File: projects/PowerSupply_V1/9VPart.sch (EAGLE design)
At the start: 10 parts, among them IC1 LM2596T, X1 IN, X3 OUT

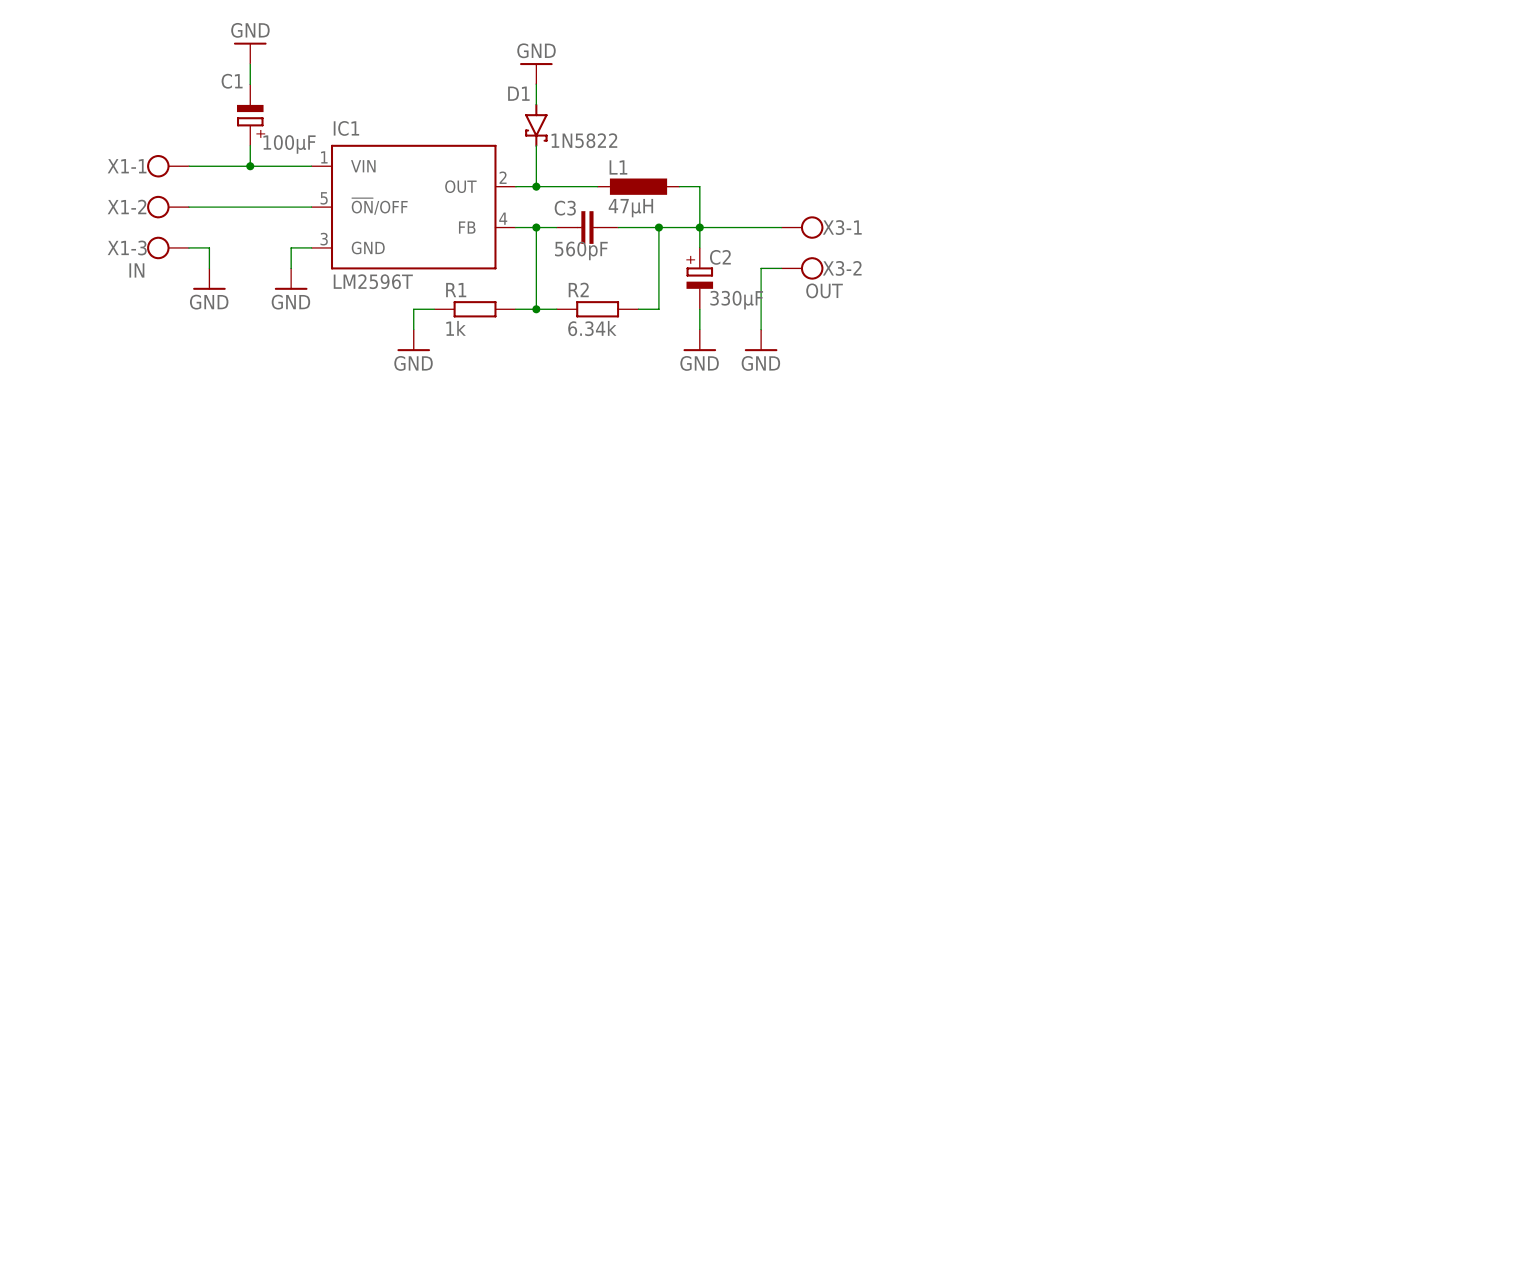
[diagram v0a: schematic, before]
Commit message: feat: power supply
changes:
- version one done
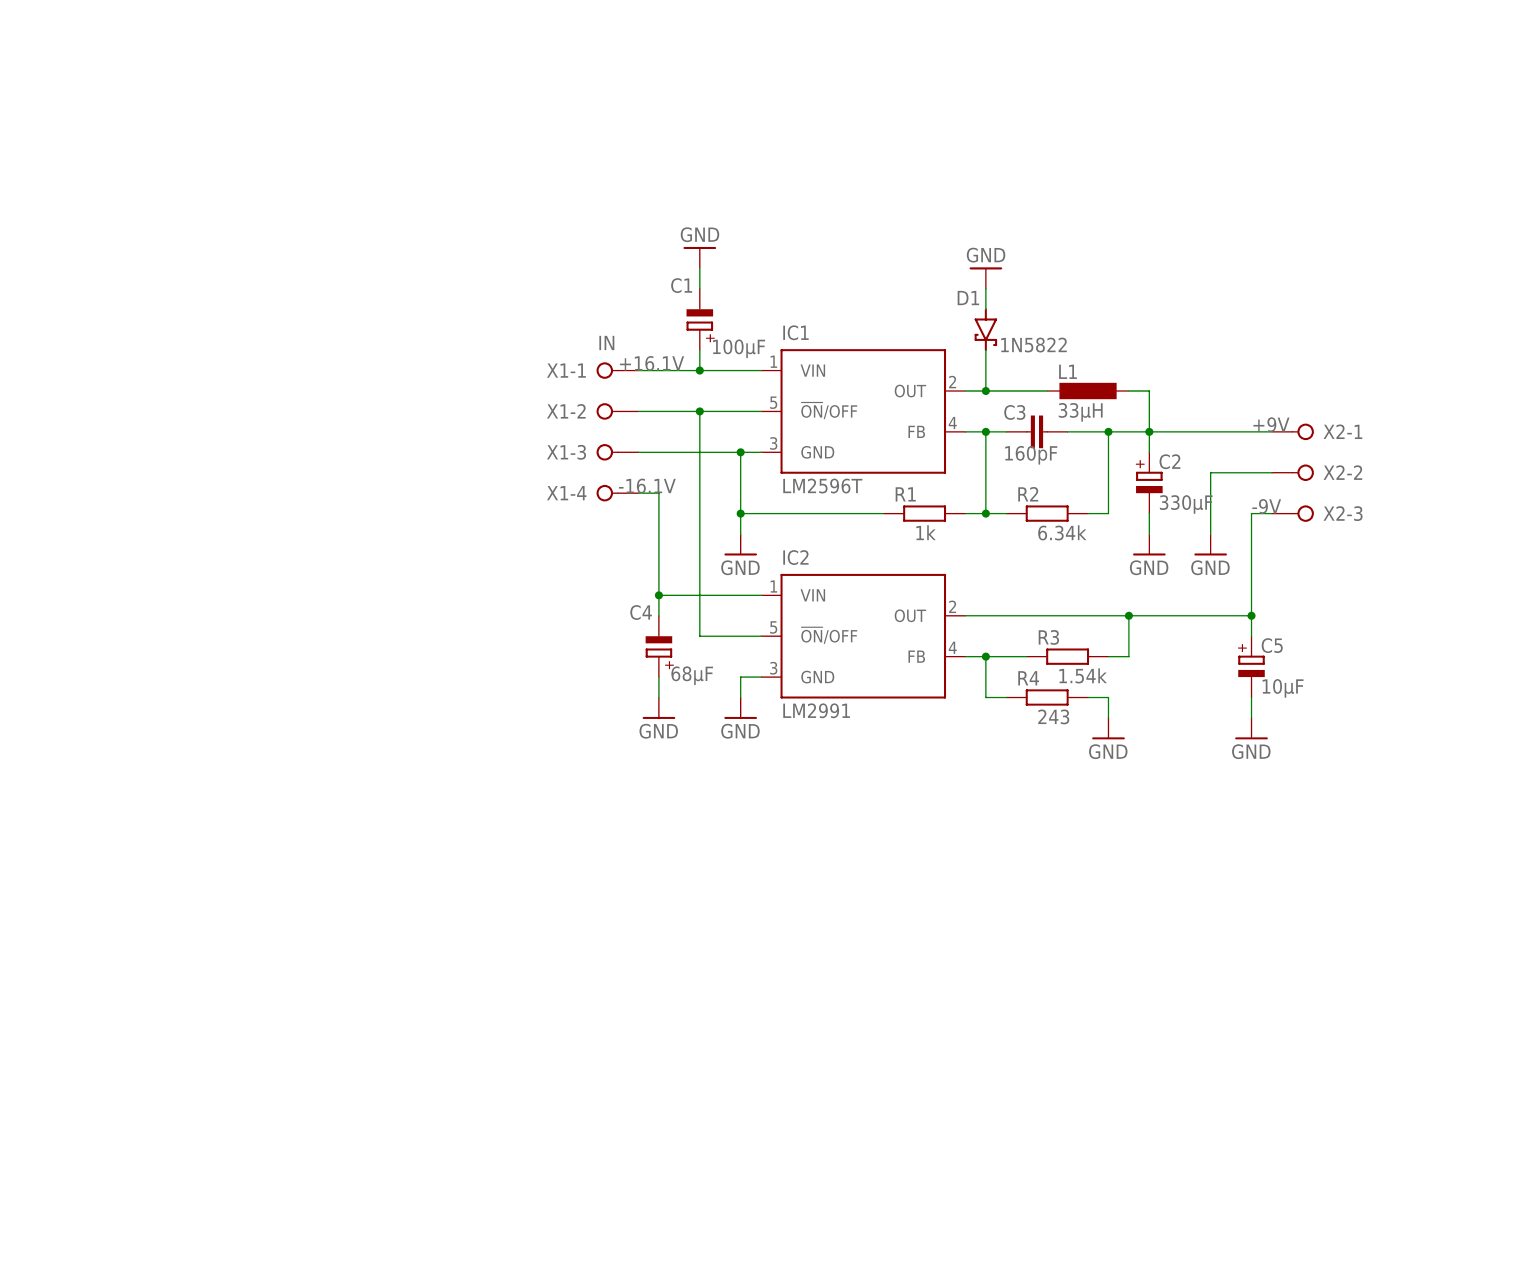
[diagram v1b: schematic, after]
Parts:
- removed X3: OUT, con-wago-500:W237-102
- added C4: 68µF, rcl:CPOL-EUE2.5-6
- added C5: 10µF, rcl:CPOL-EUE2.5-6
- added IC2: LM2991, national-semiconductor:LM2596T
- added R3: 1.54k, rcl:R-EU_0207/10
- added R4: 243, rcl:R-EU_0207/10
- added X2: (no value), con-wago-508:W237-03P
- C2: device rcl:CPOL-EUE3.5-8 -> rcl:CPOL-EUE2.5-6
- C3: value 560pF -> 160pF
- L1: value 47µH -> 33µH
- X1: device con-wago-500:W237-103 -> con-wago-508:W237-04P
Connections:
- net N$5 renamed +16.1V
- new net +9V: C2.+, C3.2, L1.1, R2.2, X2-1.KL
- new net -16.1V: C4.-, IC2.VIN, X1-4.KL
- new net -9V: C5.+, IC2.OUT, R3.2, X2-3.KL
- net GND: now also C4.+, C5.-, IC2.GND, R4.2, X2-2.KL; no longer X3-2.KL
- net N$2: now also IC2.!ON!/OFF
- net N$3: now also IC2.FB, R3.1, R4.1; no longer C2.+, C3.2, L1.1, R2.2, X3-1.KL
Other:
- moved on the sheet: C1, C2, C3, D1, IC1, L1, R1, R2

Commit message: feat: pwr fixes
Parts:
- C3: value 160pF -> 560pF
- C5: device rcl:CPOL-EUE2.5-6 -> rcl:CPOL-EUE1.8-4
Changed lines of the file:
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@@
 <part name="R1" library="rcl" library_urn="urn:adsk.eagle:library:334" deviceset="R-EU_" device="0207/10" package3d_urn="urn:adsk.eagle:package:23491/2" value="1k"/>
 <part name="R2" library="rcl" library_urn="urn:adsk.eagle:library:334" deviceset="R-EU_" device="0207/10" package3d_urn="urn:adsk.eagle:package:23491/2" value="6.34k"/>
-<part name="C3" library="rcl" library_urn="urn:adsk.eagle:library:334" deviceset="C-EU" device="050-024X044" package3d_urn="urn:adsk.eagle:package:23643/1" value="160pF"/>
+<part name="C3" library="rcl" library_urn="urn:adsk.eagle:library:334" deviceset="C-EU" device="050-024X044" package3d_urn="urn:adsk.eagle:package:23643/1" value="560pF"/>
 <part name="L1" library="rcl" library_urn="urn:adsk.eagle:library:334" deviceset="L-EU" device="TJ3-U2" package3d_urn="urn:adsk.eagle:package:23497/1" value="33µH"/>
 <part name="GND8" library="supply1" library_urn="urn:adsk.eagle:library:371" deviceset="GND" device=""/>
@@
 <part name="C4" library="rcl" library_urn="urn:adsk.eagle:library:334" deviceset="CPOL-EU" device="E2.5-6" package3d_urn="urn:adsk.eagle:package:23349/1" value="68µF"/>
 <part name="GND6" library="supply1" library_urn="urn:adsk.eagle:library:371" deviceset="GND" device=""/>
-<part name="C5" library="rcl" library_urn="urn:adsk.eagle:library:334" deviceset="CPOL-EU" device="E2.5-6" package3d_urn="urn:adsk.eagle:package:23349/1" value="10µF"/>
+<part name="C5" library="rcl" library_urn="urn:adsk.eagle:library:334" deviceset="CPOL-EU" device="E1.8-4" package3d_urn="urn:adsk.eagle:package:23336/2" value="10µF"/>
 <part name="GND7" library="supply1" library_urn="urn:adsk.eagle:library:371" deviceset="GND" device=""/>
 <part name="R3" library="rcl" library_urn="urn:adsk.eagle:library:334" deviceset="R-EU_" device="0207/10" package3d_urn="urn:adsk.eagle:package:23491/2" value="1.54k"/>

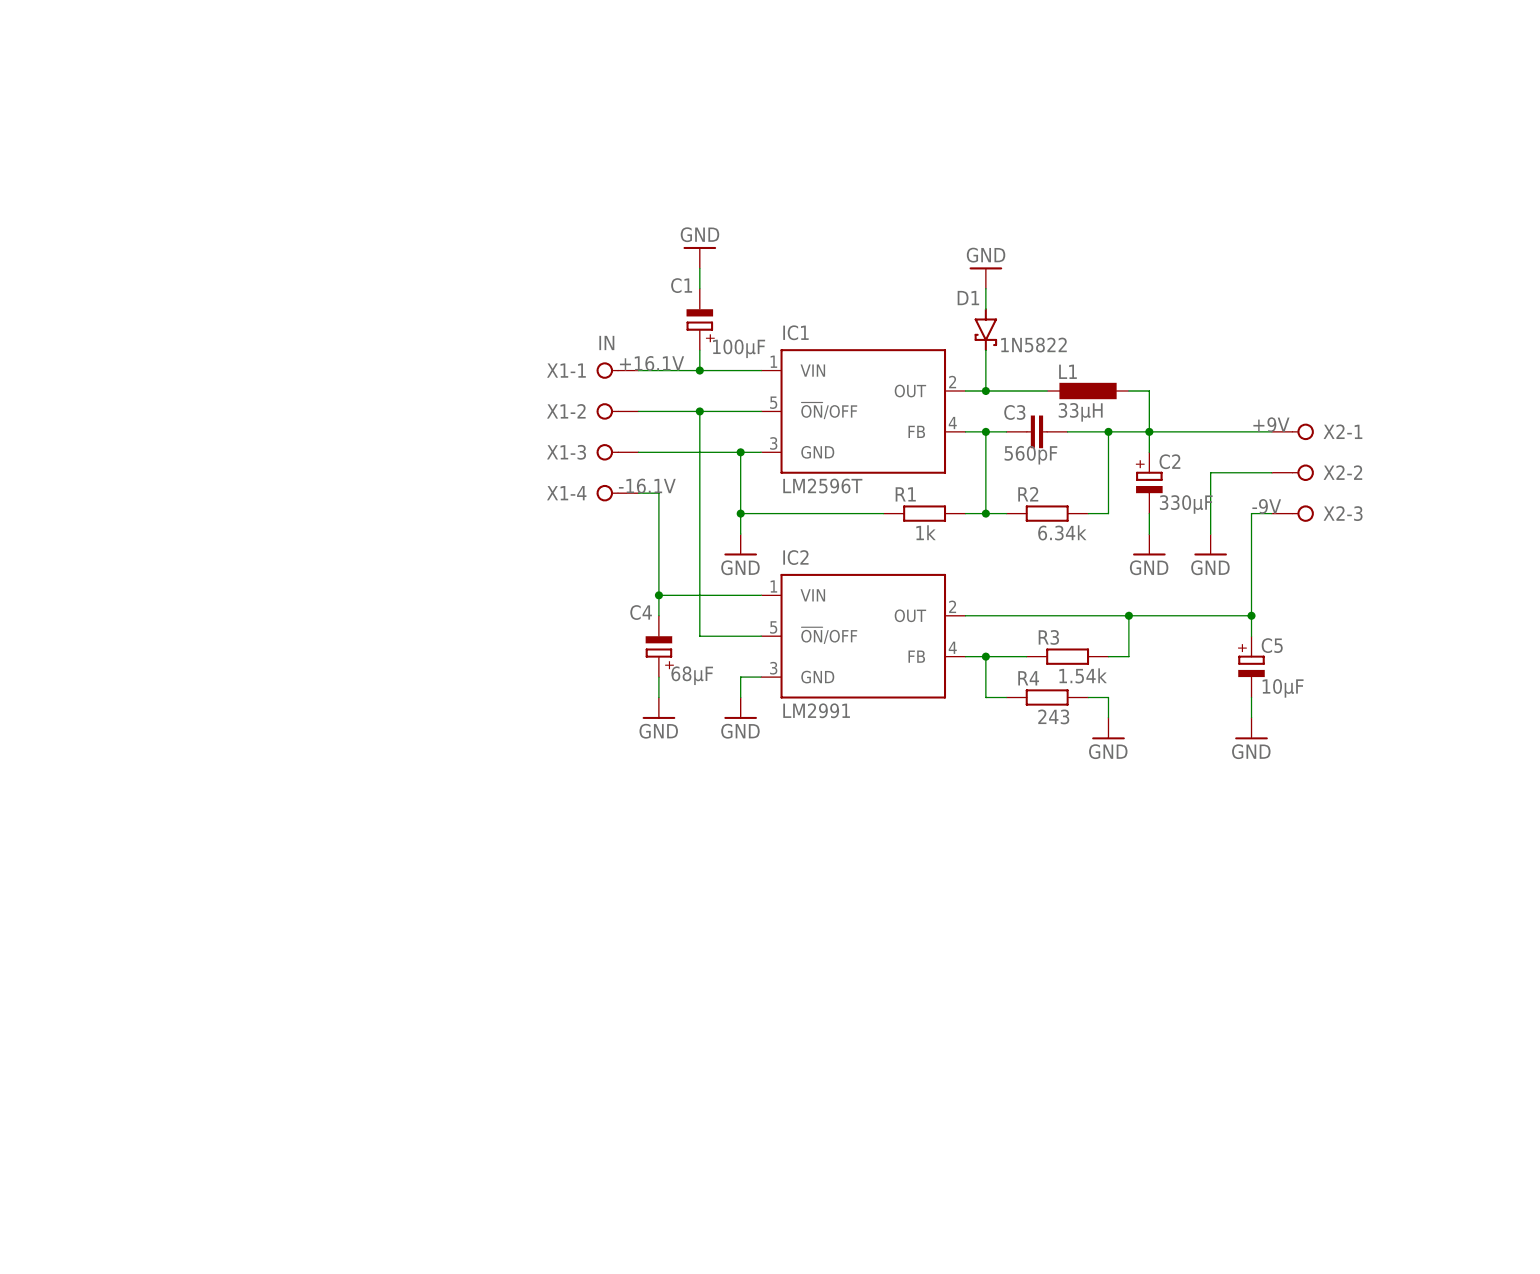
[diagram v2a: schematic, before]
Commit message: feat: 9V part refactored
changes:
- schematic changed
- layout changed
- gerber files added
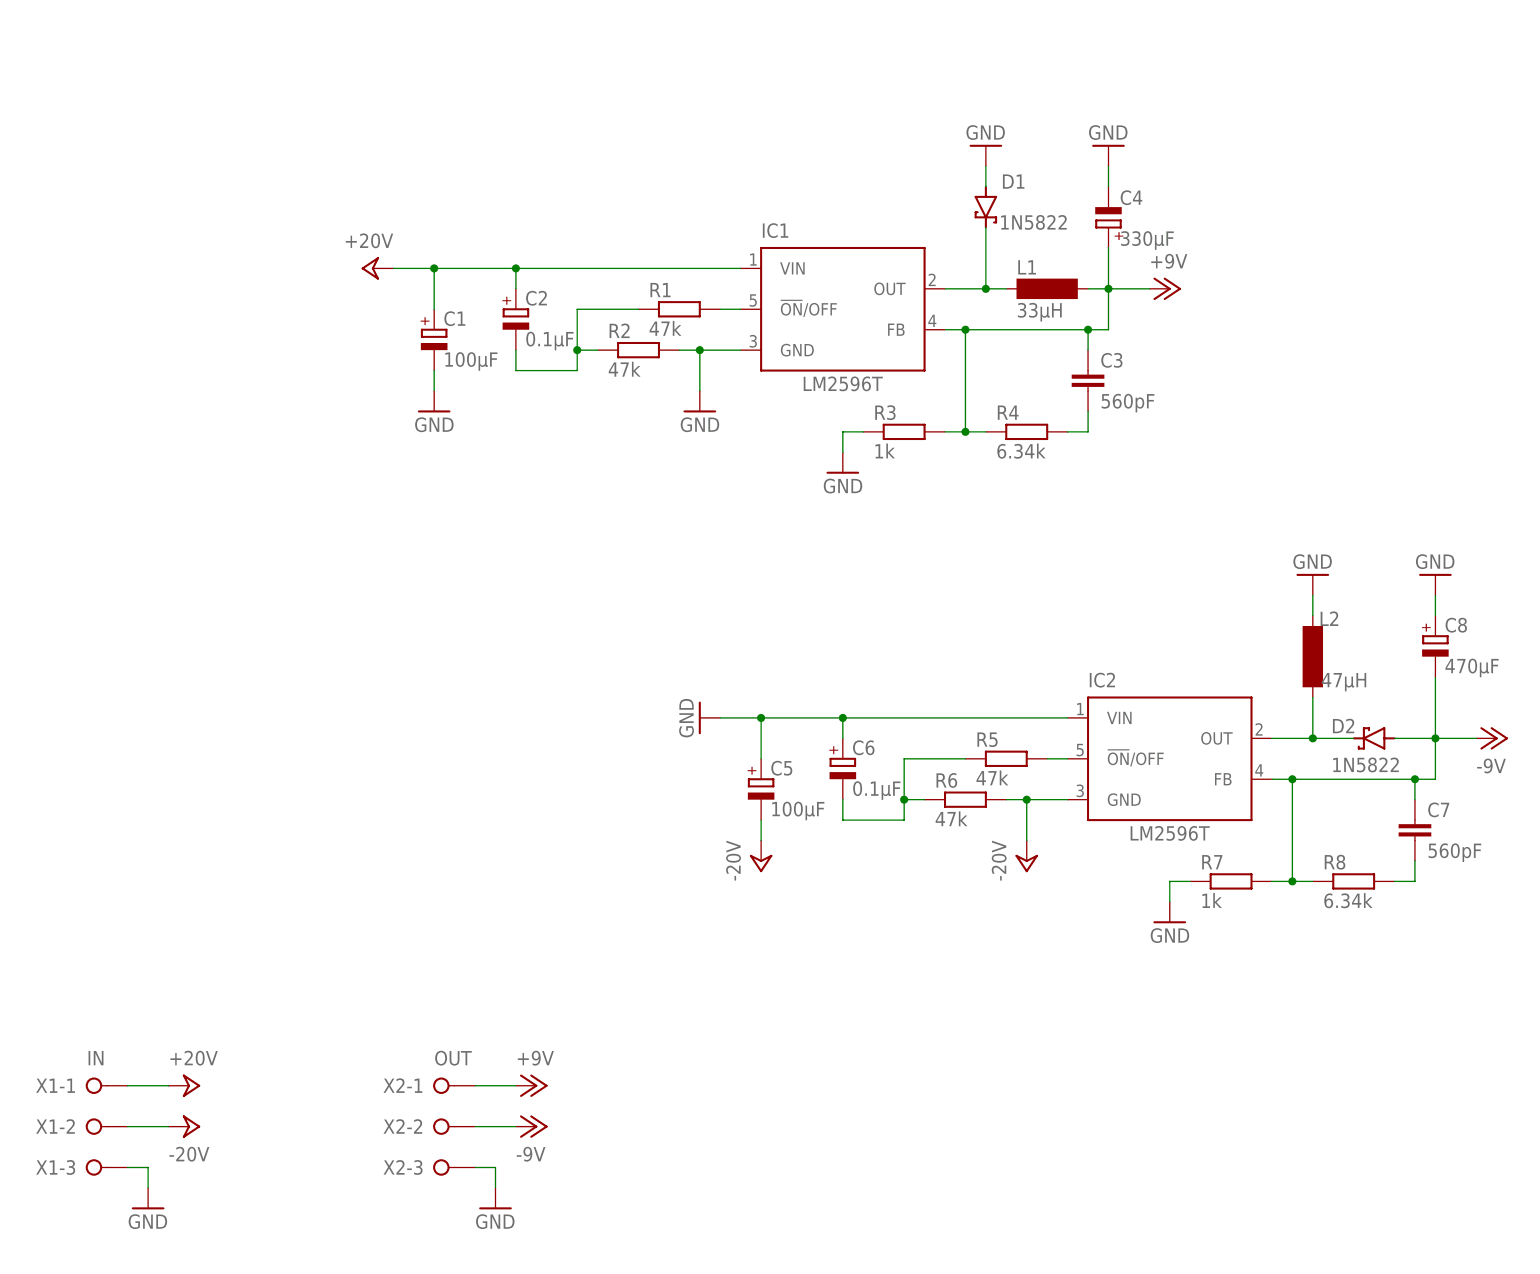
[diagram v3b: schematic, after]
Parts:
- added C6: 0.1µF, rcl:CPOL-EUE1.8-4
- added C7: 560pF, rcl:C-EU050-024X044
- added C8: 470µF, rcl:CPOL-EUE3.5-8
- added D2: 1N5822, diode:SCHOTTKY-DIODEC4111-15
- added L2: 47µH, inductor-neosid:SD12-680
- added R5, R6: 47k, rcl:R-EU_0207/10
- added R7: 1k, rcl:R-EU_0207/10
- added R8: 6.34k, rcl:R-EU_0207/10
- C2: value 330µF -> 0.1µF; device rcl:CPOL-EUE2.5-6 -> rcl:CPOL-EUE1.8-4
- C4: value 68µF -> 330µF; device rcl:CPOL-EUE2.5-6 -> rcl:CPOL-EUE3.5-8
- C5: value 10µF -> 100µF; device rcl:CPOL-EUE1.8-4 -> rcl:CPOL-EUE2.5-6
- IC2: value LM2991 -> LM2596T
- L1: device rcl:L-EUTJ3-U2 -> inductor-neosid:SD12-680
- R1: value 1k -> 47k
- R2: value 6.34k -> 47k
- R3: value 1.54k -> 1k
- R4: value 243 -> 6.34k
- X1: device con-wago-508:W237-04P -> con-wago-508:W237-03P
- X2: value (none) -> OUT
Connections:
- removed net +16.1V: C1.+, IC1.VIN, X1-1.KL
- removed net +9V: C2.+, C3.2, L1.1, R2.2, X2-1.KL
- removed net -16.1V: C4.-, IC2.VIN, X1-4.KL
- removed net -9V: C5.+, IC2.OUT, R3.2, X2-3.KL
- new net +12V: C3.1, C4.+, IC1.FB, L1.2, R3.2, R4.1, X2-1.KL
- new net +24V: C1.+, C2.+, IC1.VIN, X1-1.KL
- new net -12V: C7.1, C8.-, D2.A, IC2.FB, R7.2, R8.1, X2-2.KL
- new net -24V: C5.-, IC2.GND, R6.2, X1-2.KL
- new net N$5: C7.2, R8.2
- new net N$6: C2.-, R1.1, R2.1
- new net N$7: IC2.!ON!/OFF, R5.2
- new net N$8: C6.-, R5.1, R6.1
- net GND: now also C4.-, C5.+, C6.+, C8.+, IC2.VIN, L2.2, R2.2, R3.1, R7.1, X2-3.KL; no longer C2.-, C4.+, C5.-, IC2.GND, R1.1, R4.2, X2-2.KL
- net N$1: now also C3.2, R4.2; no longer C3.1, IC1.FB, R1.2, R2.1
- net N$2: now also D2.C, IC2.OUT, L2.1; no longer IC1.!ON!/OFF, IC2.!ON!/OFF, X1-2.KL
- net N$3: now also D1.C, IC1.OUT, L1.1; no longer IC2.FB, R3.1, R4.1
- net N$4: now also IC1.!ON!/OFF, R1.2; no longer D1.C, IC1.OUT, L1.2
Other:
- moved on the sheet: C1, C2, C3, C4, C5, D1, IC1, IC2, L1, R1, R2, R3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
